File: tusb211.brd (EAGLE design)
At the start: 42 x 20.1 mm, 11 parts, among them U1 Value

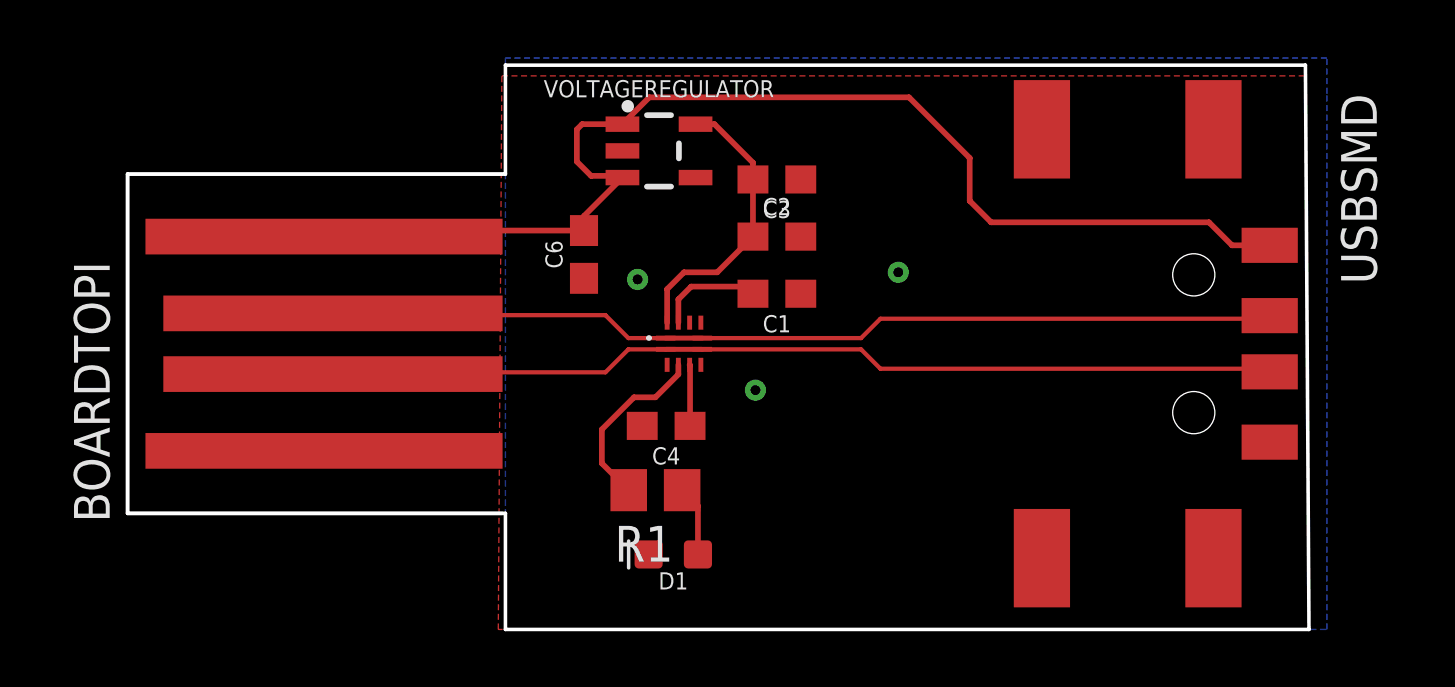
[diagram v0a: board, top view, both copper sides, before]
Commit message: changed name, fixed DRC errors
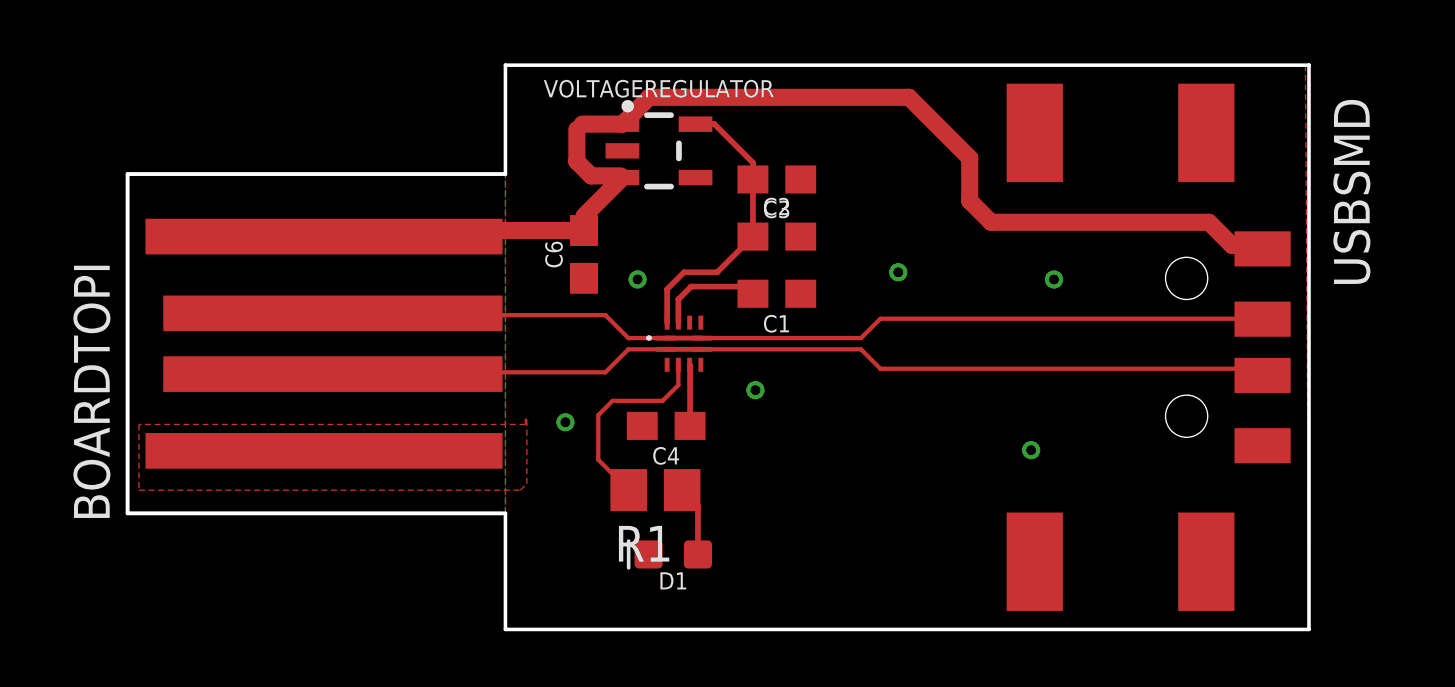
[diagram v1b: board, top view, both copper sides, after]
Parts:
- moved USBSMD 0.28 mm to (26.9, 10.0)
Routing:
- net N$3: track 6.43 -> 7.13 mm
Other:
- outline, holes or cut-outs redrawn

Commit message: Got rid of PCB USB, added led, added spot for EQ resistor, fixed wiring
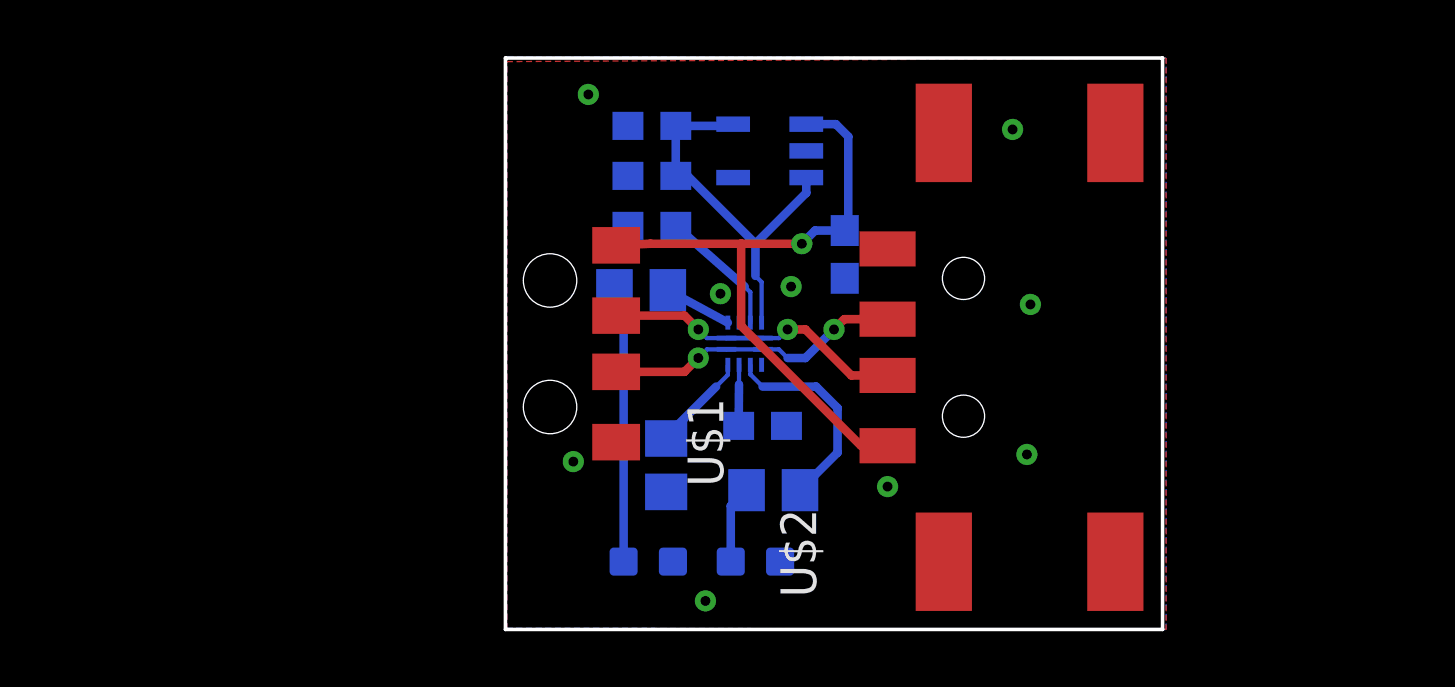
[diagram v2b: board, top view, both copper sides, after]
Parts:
- removed BOARDTOPI: USBPCB, USBPCB:USBPCB
- removed USBSMD: USB, USBSMD:USBSMD
- added D2: GREEN, SparkFun-LED:LED-0603
- added R2, VARIABLER: 120, rcl:R0805
- added U$1: TYPEAUSB, TYPEAUSBSMDMALE:TYPEAUSB
- added U$2: USB, USBSMD:USBSMD
- moved C6 9.27 mm to (12.1, 13.3), flipped to the bottom
- moved C1 5.06 mm to (5.21, 14.4), flipped to the bottom
- moved C2 4.94 mm to (5.21, 16.1), flipped to the bottom
- moved C3 4.84 mm to (5.21, 17.9), flipped to the bottom
- moved R1 4.19 mm to (9.53, 4.95), flipped to the bottom
- moved VOLTAGEREGULATOR 3.94 mm to (9.40, 17.0), flipped to the bottom
- moved C4 3.43 mm to (9.14, 7.24), flipped to the bottom
- moved D1 2.93 mm to (8.89, 2.41), flipped to the bottom
- moved U1 2.16 mm to (8.51, 10.2), flipped to the bottom
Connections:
- removed net EQ: U1.6
- new net N$5: U1.6, VARIABLER.2
- new net N$6: R2.2, U1.9
- new net N$7: D2.A, R2.1
- net 3.3V: now also VOLTAGEREGULATOR.3
- net GND: now also D2.C, U$1.GND, U$2.P$4, VARIABLER.1; no longer BOARDTOPI.4, USBSMD.P$4
- net M: now also U$1.D-, U$2.P$2; no longer BOARDTOPI.2, USBSMD.P$2
- net P: now also U$1.D+, U$2.P$3; no longer BOARDTOPI.3, USBSMD.P$3
- net VIN: now also U$1.VCC, U$2.P$1; no longer BOARDTOPI.1, USBSMD.P$1, VOLTAGEREGULATOR.3
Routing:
- net P: track 34.1 -> 10.7 mm, vias 0 -> 2
- net M: track 34.0 -> 10.8 mm, vias 0 -> 2
- net VIN: track 42.7 -> 23.3 mm, vias 0 -> 1
- net N$7: track 0.00 -> 9.79 mm
- net N$5: track 0.00 -> 3.53 mm
- net 3.3V: track 10.3 -> 13.7 mm
- net N$6: track 0.00 -> 2.43 mm
- net N$1: track 3.77 -> 4.63 mm
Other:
- board size 42 x 20.1 mm -> 23.4 x 20.3 mm

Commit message: changed trace widths
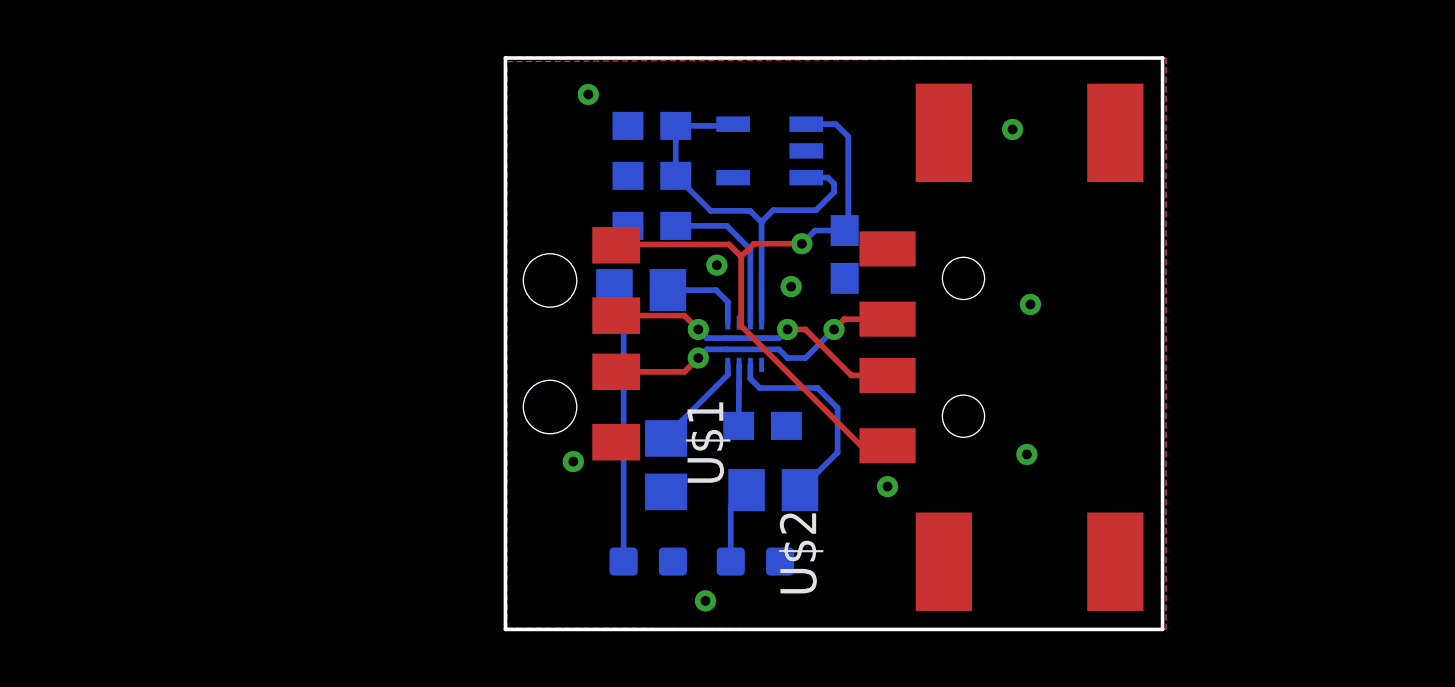
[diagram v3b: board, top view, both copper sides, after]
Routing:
- net 3.3V: track 13.7 -> 15.6 mm
- net N$1: track 4.63 -> 5.60 mm
- net N$6: track 2.43 -> 3.04 mm

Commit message: D+ and D- have same length
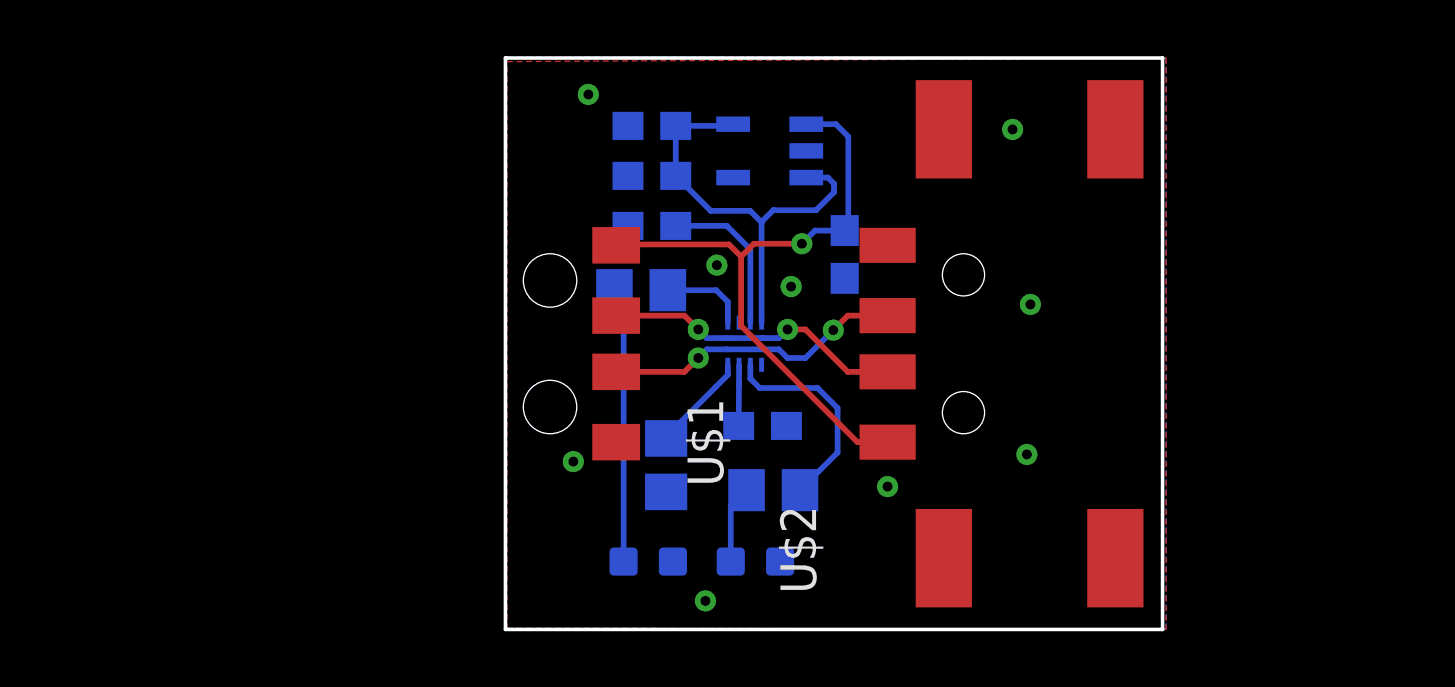
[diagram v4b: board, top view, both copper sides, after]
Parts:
- moved U$2 0.13 mm to (13.6, 10.2)
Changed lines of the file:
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@@
 <attribute name="PROD_ID" value="DIO-00821" x="5.08" y="2.413" size="1.778" layer="28" rot="MR180" display="off"/>
 </element>
-<element name="U$2" library="USBSMD" package="USBSMD" value="USB" x="13.589" y="10.033" rot="R90"/>
+<element name="U$2" library="USBSMD" package="USBSMD" value="USB" x="13.589" y="10.16" rot="R90"/>
 </elements>
 <signals>
@@
 <via x="18.034" y="17.78" extent="1-16" drill="0.35"/>
 <via x="7.112" y="1.016" extent="1-16" drill="0.35"/>
-<wire x1="7.5184" y1="12.954" x2="8.309" y2="10.91" width="0" layer="19" extent="16-16"/>
 </signal>
 <signal name="N$1">
@@
 <contactref element="U$2" pad="P$3"/>
 <wire x1="10.033" y1="9.652" x2="9.725" y2="9.96" width="0.2032" layer="16"/>
-<wire x1="10.668" y1="9.652" x2="11.684" y2="10.668" width="0.2032" layer="16"/>
-<via x="11.684" y="10.668" extent="1-16" drill="0.35"/>
 <wire x1="10.033" y1="9.652" x2="10.668" y2="9.652" width="0.2032" layer="16"/>
 <wire x1="7.859" y1="9.96" x2="7.166" y2="9.96" width="0.2032" layer="16"/>
@@
 <wire x1="9.725" y1="9.96" x2="9.159" y2="9.96" width="0.2032" layer="16"/>
 <wire x1="9.159" y1="9.96" x2="7.859" y2="9.96" width="0.2032" layer="16"/>
-<wire x1="11.684" y1="10.668" x2="12.049" y2="11.033" width="0.2032" layer="1"/>
-<wire x1="12.049" y1="11.033" x2="13.589" y2="11.033" width="0.2032" layer="1"/>
+<wire x1="10.668" y1="9.652" x2="11.65895625" y2="10.64295625" width="0.2032" layer="16"/>
+<via x="11.65895625" y="10.64295625" extent="1-16" drill="0.35"/>
+<wire x1="11.65895625" y1="10.64295625" x2="12.176" y2="11.16" width="0.2032" layer="1"/>
+<wire x1="12.176" y1="11.16" x2="13.589" y2="11.16" width="0.2032" layer="1"/>
 </signal>
 <signal name="M">
@@
 <via x="10.033" y="10.668" extent="1-16" drill="0.35"/>
 <wire x1="10.033" y1="10.668" x2="10.668" y2="10.668" width="0.2032" layer="1"/>
-<wire x1="12.303" y1="9.033" x2="13.589" y2="9.033" width="0.2032" layer="1"/>
-<wire x1="10.668" y1="10.668" x2="12.303" y2="9.033" width="0.2032" layer="1"/>
+<wire x1="10.668" y1="10.668" x2="12.176" y2="9.16" width="0.2032" layer="1"/>
+<wire x1="12.176" y1="9.16" x2="13.589" y2="9.16" width="0.2032" layer="1"/>
 </signal>
 <signal name="VIN">
@@
 <via x="10.541" y="13.716" extent="1-16" drill="0.35"/>
 <contactref element="U$2" pad="P$1"/>
-<wire x1="12.644" y1="6.533" x2="8.382" y2="10.795" width="0.2032" layer="1"/>
-<wire x1="12.644" y1="6.533" x2="13.589" y2="6.533" width="0.2032" layer="1"/>
-<wire x1="8.382" y1="10.795" x2="8.382" y2="13.2588" width="0.2032" layer="1"/>
+<wire x1="8.382" y1="13.2588" x2="8.382" y2="10.795" width="0.2032" layer="1"/>
 <wire x1="8.382" y1="13.2588" x2="7.9502" y2="13.6906" width="0.2032" layer="1"/>
 <wire x1="8.382" y1="13.2588" x2="8.8392" y2="13.716" width="0.2032" layer="1"/>
@@
 <wire x1="3.9676" y1="13.6906" x2="3.937" y2="13.66" width="0.2032" layer="1" curve="90"/>
 <wire x1="7.9502" y1="13.6906" x2="3.9676" y2="13.6906" width="0.2032" layer="1"/>
+<wire x1="8.382" y1="10.795" x2="12.517" y2="6.66" width="0.2032" layer="1"/>
+<wire x1="12.517" y1="6.66" x2="13.589" y2="6.66" width="0.2032" layer="1"/>
 </signal>
 <signal name="NC/ADJ">
